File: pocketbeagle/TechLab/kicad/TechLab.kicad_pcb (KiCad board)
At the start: 2 copper layers, 111.5 x 55.8 mm, 94 parts, among them J2 USB_C_Receptacle_USB2.0, J4 Conn_01x02, P1 Conn_02x18_Odd_Even, P2 Conn_02x18_Odd_Even, T1 3904, T2 EAALSTIC1708A0, U1 CAT24C32, U2 TPD4S012DRY, U3 MMA8453Q, U4 TPS2051CDBV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

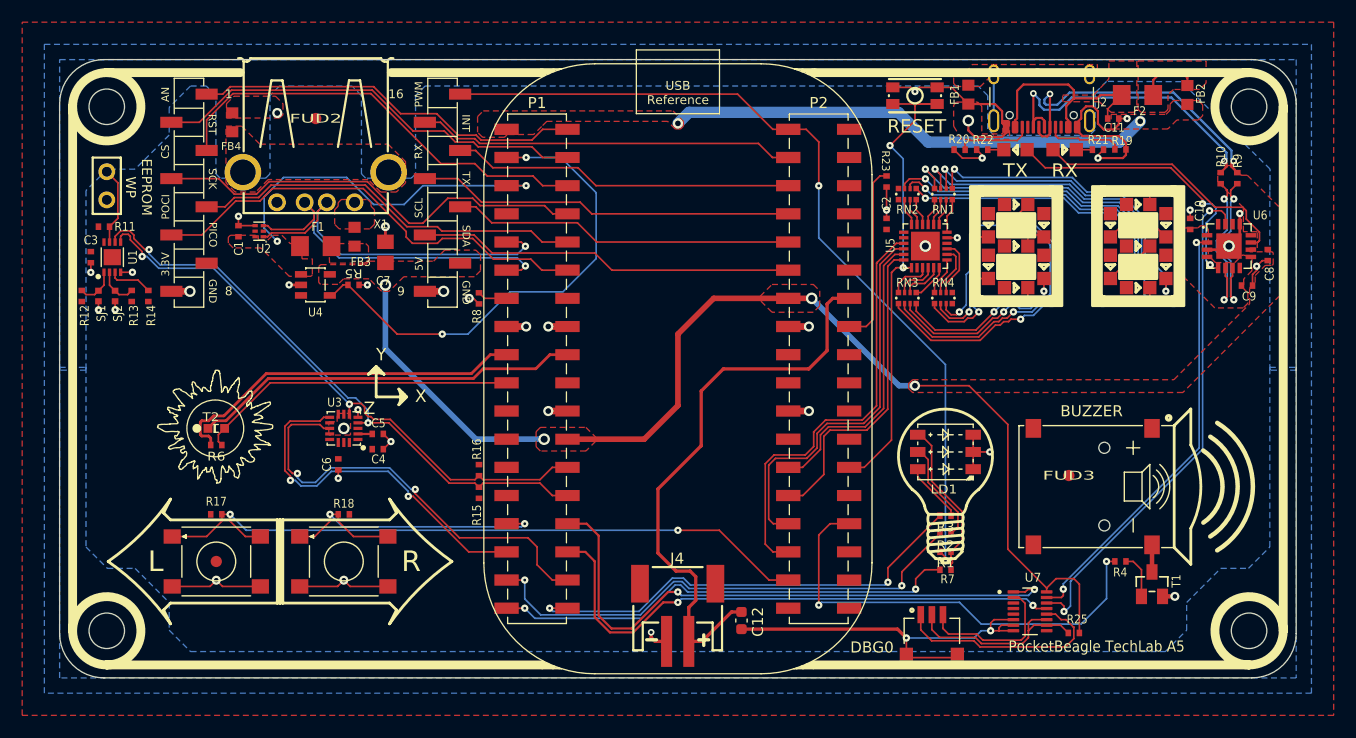
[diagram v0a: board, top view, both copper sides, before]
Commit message: Update cape header pins slinkscreen front and back
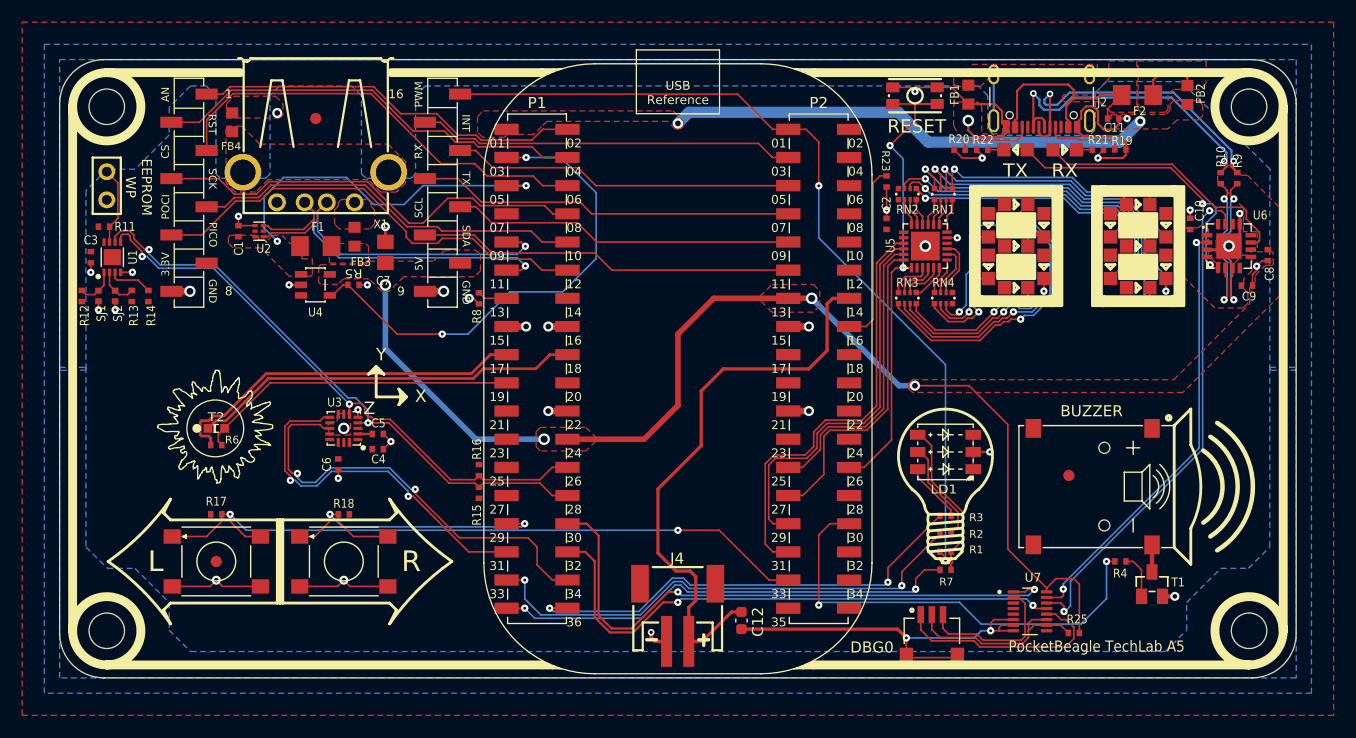
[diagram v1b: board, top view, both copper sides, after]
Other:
- board text added: "01"
- board text added: "02"
- board text added: "03"
- board text added: "04"
- board text added: "05"
- board text added: "06"
- board text added: "07"
- board text added: "08"
- board text added: "09"
- board text added: "10"
- board text added: "11"
- board text added: "12"
- board text added: "13"
- board text added: "14"
- board text added: "15"
- board text added: "17"
- board text added: "18"
- board text added: "19"
- board text added: "20"
- board text added: "21"
- board text added: "22"
- board text added: "23"
- board text added: "24"
- board text added: "25"
- board text added: "26"
- board text added: "27"
- board text added: "28"
- board text added: "29"
- board text added: "30"
- board text added: "31"
- board text added: "32"
- board text added: "33"
- board text added: "34"
- board text added: "35"
- board text added: "36"
- board text added: "GPIO Inputs Right Button P1.29 Left Button P2.33 Analog Inputs Light Sensor P1.19 GPIO/PWM Outputs LED Red P1.33 LED Green P2.01 LED Blue P1.36 Buzzer P2.30"
- board text added: "SPI MCP23S18 GPO CS P2.31 SCK P2.29 POCI P2.27 PICO P2.25"
- board text added: "mikroBUS AN P1.02 PWM P2.01 RST P1.04 INT P2.03 CS P1.06 RX P2.05 SCK P1.08 TX P2.07 POCI P1.10 SCL P2.09 PICO P1.12 SDA P2.11 USB UART FT230XQ TX P1.32 RX P1.30 I2C MMA8453Q Accel 0x1C CAT24C32 EEPROM 0x57 SDA P1.26 SCL P1.28"
- board text removed: "GPIO Inputs Right Button 129 Left Button 233 Analog Inputs Light Sensor 119 GPIO/PWM Outputs LED Red 133 LED Green 201 LED Blue 136 Buzzer 230"
- board text removed: "SPI MCP23S18 GPO CS 231 SCK 229 POCI 227 PICO 225"
- board text removed: "mikroBUS AN 102 PWM 201 RST 104 INT 203 CS 106 RX 205 SCK 108 TX 207 POCI 110 SCL 209 PICO 112 SDA 211 USB UART FT230XQ TX 132 RX 130 I2C MMA8453Q Accel 0x1C CAT24C32 EEPROM 0x57 SDA 126 SCL 128"

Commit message: Add I2C port
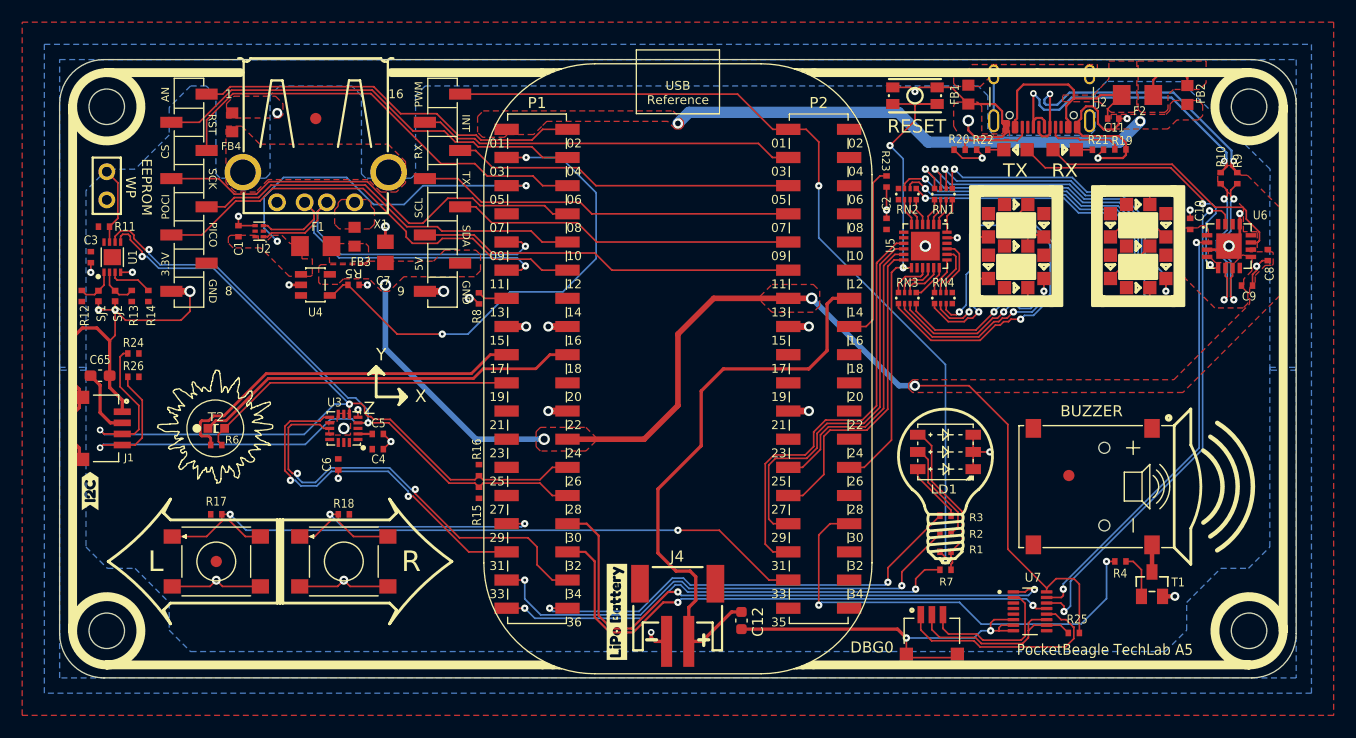
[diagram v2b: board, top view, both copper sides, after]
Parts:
- added C65: 1uF, Capacitor_SMD:C_0603_1608Metric_Pad1.08x0.95mm_HandSolder, F.Cu at (151.9, 78.0)
- added J1: JST-SH-4P, Upside Down Labs:JST-SH-4P, F.Cu at (151.9, 82.8)
- added R24: 4.7k, 0402, F.Cu at (154.9, 76.0)
- added R26: 4.7k, 0402, F.Cu at (154.9, 78.1)
- added kibuzzard-68396DBE: G***, kibuzzard-68396DBE, F.Cu at (151.0, 88.4)
- added kibuzzard-68396DE6: G***, kibuzzard-68396DE6, F.Cu at (198.5, 99.3)
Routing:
- net P1.26(I2C2.SDA): track 52.5 -> 88.2 mm, vias 2 -> 3
- net P1.28(I2C2.SCL): track 53.7 -> 89.3 mm, vias 2 -> 3
- net GND: track 139.1 -> 173.0 mm, vias 40 -> 42
- net 3.3V: track 0.00 -> 6.07 mm

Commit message: PCB minor updates
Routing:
- net GND: track 173.0 -> 174.5 mm
- net VOUT: track 101.3 -> 102.4 mm
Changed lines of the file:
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@@
 			(outputformat 1)
 			(mirror no)
-			(drillshape 1)
+			(drillshape 0)
 			(scaleselection 1)
-			(outputdirectory "")
+			(outputdirectory "gerbers")
 		)
 	)
@@
 				(font
 					(size 0.001 0.001)
+					(thickness 0.15)
 				)
 			)
@@
 				(font
 					(size 0.001 0.001)
+					(thickness 0.15)
 				)
 			)
@@
 				(font
 					(size 0.001 0.001)
+					(thickness 0.15)
 				)
 			)
@@
 				(font
 					(size 0.001 0.001)
+					(thickness 0.15)
 				)
 			)
@@
 	)
 	(segment
+		(start 150.4 81.25)
+		(end 150.025 80.875)
+		(width 0.3)
+		(layer "F.Cu")
+		(net 1)
+	)
+	(segment
 		(start 254.6636 64.3411)
 		(end 254.6636 65.3411)
@@
 	)
 	(segment
+		(start 151.25 81.25)
+		(end 150.4 81.25)
+		(width 0.3)
+		(layer "F.Cu")
+		(net 1)
+	)
+	(segment
 		(start 225.0011 52.0036)
 		(end 225.3761 52.3786)
@@
 	)
 	(segment
+		(start 150.025 84.525)
+		(end 150.025 85.5536)
+		(width 0.3)
+		(layer "F.Cu")
+		(net 1)
+	)
+	(segment
 		(start 229.65 58.3786)
 		(end 231.4386 58.3786)
@@
 	)
 	(segment
+		(start 150.025 80.875)
+		(end 150.025 79.9536)
+		(width 0.3)
+		(layer "F.Cu")
+		(net 1)
+	)
+	(segment
 		(start 230.6261 84.8786)
 		(end 230.6261 86.4286)
@@
 	)
 	(segment
-		(start 150.025 80.875)
-		(end 149.5 81.4)
-		(width 0.3)
-		(layer "F.Cu")
-		(net 1)
-	)
-	(segment
 		(start 223.3761 52.0036)
 		(end 225.0011 52.0036)
@@
 	)
 	(segment
-		(start 154.185 73)
-		(end 159.2 73)
-		(width 0.1524)
+		(start 151.3 83.73)
+		(end 150.82 83.73)
+		(width 0.3)
 		(layer "F.Cu")
 		(net 1)
 	)
 	(segment
-		(start 150.025 85.5536)
-		(end 150.025 84.525)
-		(width 0.3)
+		(start 154.185 73)
+		(end 159.2 73)
+		(width 0.1524)
 		(layer "F.Cu")
 		(net 1)
@@
 	)
 	(segment
-		(start 150.025 84.525)
-		(end 149.5 84)
-		(width 0.3)
-		(layer "F.Cu")
-		(net 1)
-	)
-	(segment
 		(start 240 55.59)
 		(end 240 55.166)
@@
 	)
 	(segment
-		(start 150.025 79.9536)
-		(end 150.025 80.875)
-		(width 0.3)
-		(layer "F.Cu")
-		(net 1)
-	)
-	(segment
 		(start 243.7511 54.8161)
 		(end 244.5011 54.8161)
@@
 	)
 	(segment
+		(start 150.82 83.73)
+		(end 150.025 84.525)
+		(width 0.3)
+		(layer "F.Cu")
+		(net 1)
+	)
+	(segment
 		(start 175.2511 69.8161)
 		(end 176.0011 69.8161)
@@
 	)
 	(via
-		(at 149.5 84)
+		(at 151.3 83.73)
 		(size 0.6)
 		(drill 0.3)
@@
 	)
 	(via
-		(at 149.5 81.4)
+		(at 151.25 81.25)
 		(size 0.6)
 		(drill 0.3)
@@
 	)
 	(segment
-		(start 239.6796 100.6796)
-		(end 239.7 100.7)
+		(start 226.8808 101.9058)
+		(end 225.9 100.925)
 		(width 0.1524)
 		(layer "F.Cu")
@@
 	)
 	(segment
-		(start 238.9476 102.4616)
-		(end 231.246668 102.4616)
+		(start 231.246668 102.4616)
+		(end 230.690868 101.9058)
 		(width 0.1524)
 		(layer "F.Cu")
@@
 	)
 	(segment
-		(start 231.246668 102.4616)
-		(end 230.690868 101.9058)
+		(start 230.690868 101.9058)
+		(end 226.8808 101.9058)
 		(width 0.1524)
 		(layer "F.Cu")
@@
 	)
 	(segment
-		(start 225.9 100.925)
-		(end 225.9 99.55)
+		(start 238.9476 102.4616)
+		(end 231.246668 102.4616)
 		(width 0.1524)
 		(layer "F.Cu")
@@
 	)
 	(segment
-		(start 239 100)
-		(end 239.6704 100.6704)
+		(start 238.46 100)
+		(end 239 100)
 		(width 0.1524)
 		(layer "F.Cu")
@@
 	)
 	(segment
-		(start 239.7 100.7)
-		(end 239.7 101.7092)
+		(start 239.6796 100.6704)
+		(end 239.6796 100.6796)
 		(width 0.1524)
 		(layer "F.Cu")
@@
 	)
 	(segment
-		(start 230.690868 101.9058)
-		(end 226.8808 101.9058)
+		(start 239.6704 100.6704)
+		(end 239.6796 100.6704)
 		(width 0.1524)
 		(layer "F.Cu")
@@
 	)
 	(segment
-		(start 237.25 99.5)
-		(end 238.05 99.5)
+		(start 239 100)
+		(end 239.6704 100.6704)
 		(width 0.1524)
 		(layer "F.Cu")
@@
 	)
 	(segment
-		(start 239.6796 100.6704)
-		(end 239.6796 100.6796)
+		(start 225.9 100.925)
+		(end 225.9 99.55)
 		(width 0.1524)
 		(layer "F.Cu")
@@
 	)
 	(segment
-		(start 239.6704 100.6704)
-		(end 239.6796 100.6704)
+		(start 237.25 99.5)
+		(end 237.96 99.5)
 		(width 0.1524)
 		(layer "F.Cu")
@@
 	)
 	(segment
-		(start 238.05 99.5)
-		(end 238.55 100)
+		(start 239.6796 100.6796)
+		(end 239.7 100.7)
 		(width 0.1524)
 		(layer "F.Cu")
@@
 	)
 	(segment
-		(start 239.7 101.7092)
-		(end 238.9476 102.4616)
+		(start 237.96 99.5)
+		(end 238.46 100)
 		(width 0.1524)
 		(layer "F.Cu")
@@
 	)
 	(segment
-		(start 238.55 100)
-		(end 239 100)
+		(start 239.7 101.7092)
+		(end 238.9476 102.4616)
 		(width 0.1524)
 		(layer "F.Cu")
@@
 	)
 	(segment
-		(start 226.8808 101.9058)
-		(end 225.9 100.925)
+		(start 239.7 100.7)
+		(end 239.7 101.7092)
 		(width 0.1524)
 		(layer "F.Cu")
@@
 	)
 	(segment
-		(start 233.75 93.65)
-		(end 233.75 82.4)
-		(width 0.1524)
-		(layer "F.Cu")
-		(net 45)
-	)
-	(segment
 		(start 240.2 96.8)
 		(end 239.7 96.3)
@@
 	)
 	(segment
-		(start 237.25 97.15)
-		(end 233.75 93.65)
-		(width 0.1524)
-		(layer "F.Cu")
-		(net 45)
-	)
-	(segment
 		(start 239.7 96.3)
 		(end 238.1 96.3)
@@
 	)
 	(segment
+		(start 233.75 94.65)
+		(end 233.75 82.4)
+		(width 0.1524)
+		(layer "F.Cu")
+		(net 45)
+	)
+	(segment
 		(start 240.2 101.2)
 		(end 240.2 96.8)
@@
 	)
 	(segment
-		(start 204.0011 74.2536)
-		(end 204.0011 80.6911)
-		(width 0.508)
+		(start 230.2536 78.9036)
+		(end 225.3761 78.9036)
+		(width 0.1524)
 		(layer "F.Cu")
 		(net 45)
 	)
 	(segment
-		(start 200.9636 83.7286)
+		(start 238.1 96.3)
+		(end 235.4 96.3)
+		(width 0.1524)
+		(layer "F.Cu")
+		(net 45)
+	)
+	(segment
+		(start 204.0011 74.2536)
 		(end 204.0011 80.6911)
 		(width 0.508)
@@
 	)
 	(segment
-		(start 237.25 97.15)
-		(end 237.25 97.5)
+		(start 235.4 96.3)
+		(end 233.75 94.65)
 		(width 0.1524)
 		(layer "F.Cu")
@@
 	)
 	(segment
-		(start 230.2536 78.9036)
-		(end 225.3761 78.9036)
+		(start 200.9636 83.7286)
+		(end 204.0011 80.6911)
+		(width 0.508)
+		(layer "F.Cu")
+		(net 45)
+	)
+	(segment
+		(start 237.25 97.15)
+		(end 237.25 97.5)
 		(width 0.1524)
 		(layer "F.Cu")
@@
 	)
 	(segment
-		(start 235.6089 97.8161)
+		(start 234.7339 97.8161)
 		(end 204.3136 97.8161)
 		(width 0.1524)
@@
 	)
 	(segment
-		(start 204.3136 97.8161)
-		(end 204.0011 97.5036)
+		(start 235.275 97.275)
+		(end 234.7339 97.8161)
 		(width 0.1524)
 		(layer "B.Cu")
@@
 	(segment
 		(start 236.15 97.275)
-		(end 235.6089 97.8161)
+		(end 235.275 97.275)
+		(width 0.1524)
+		(layer "B.Cu")
+		(net 122)
+	)
+	(segment
+		(start 204.3136 97.8161)
+		(end 204.0011 97.5036)
 		(width 0.1524)
 		(layer "B.Cu")
@@
 	(segment
 		(start 236.0125 98.7125)
-		(end 235.4286 98.1286)
+		(end 235.2425 98.7125)
 		(width 0.1524)
 		(layer "B.Cu")
@@
 	)
 	(segment
-		(start 235.4286 98.1286)
-		(end 204.3136 98.1286)
+		(start 204.3136 98.1286)
+		(end 204.0011 98.4411)
 		(width 0.1524)
 		(layer "B.Cu")
@@
 	)
 	(segment
-		(start 204.3136 98.1286)
-		(end 204.0011 98.4411)
+		(start 235.2425 98.7125)
+		(end 234.6586 98.1286)
+		(width 0.1524)
+		(layer "B.Cu")
+		(net 131)
+	)
+	(segment
+		(start 234.6586 98.1286)
+		(end 204.3136 98.1286)
 		(width 0.1524)
 		(layer "B.Cu")
